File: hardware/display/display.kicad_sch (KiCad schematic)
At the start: 0 parts

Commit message: Started Display Layout
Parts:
- added C1, C10, C11, C12, C13, C14, C15, C16, C17, C18, C19, C2, C20, C21, C22, C23, C24, C25, C26, C27, C28, C29, C3, C30, C31, C32, C33, C34, C35, C36, C37, C38, C39, C4, C40, C41, C42, C43, C44, C45, C46, C47, C48, C49, C5, C50, C51, C52, C53, C54, C55, C56, C57, C58, C59, C6, C60, C61, C62, C63, C64, C65, C66, C67, C68, C69, C7, C70, C71, C72, C73, C74, C75, C76, C77, C78, C79, C8, C80, C9: 0.1uF, Capacitor_SMD:C_0504_1310Metric_Pad0.83x1.28mm_HandSolder, symbol Device:C_Small
- added C81: 1000uF, esp32_handheld:EEEFK0J332AQ, symbol Device:C_Polarized_Small_US
- added D1, D10, D100, D101, D102, D103, D104, D105, D106, D107, D108, D109, D11, D110, D111, D112, D113, D114, D115, D116, D117, D118, D119, D12, D120, D121, D122, D123, D124, D125, D126, D127, D128, D129, D13, D130, D131, D132, D133, D134, D135, D136, D137, D138, D139, D14, D140, D141, D142, D143, D144, D145, D146, D147, D148, D149, D15, D150, D151, D152, D153, D154, D155, D156, D157, D158, D159, D16, D160, D161, D162, D163, D164, D165, D166, D167, D168, D169, D17, D170, D171, D172, D173, D174, D175, D176, D177, D178, D179, D18, D180, D181, D182, D183, D184, D185, D186, D187, D188, D189, D19, D190, D191, D192, D193, D194, D195, D196, D197, D198, D199, D2, D20, D200, D201, D202, D203, D204, D205, D206, D207, D208, D209, D21, D210, D211, D212, D213, D214, D215, D216, D217, D218, D219, D22, D220, D221, D222, D223, D224, D225, D226, D227, D228, D229, D23, D230, D231, D232, D233, D234, D235, D236, D237, D238, D239, D24, D240, D241, D242, D243, D244, D245, D246, D247, D248, D249, D25, D250, D251, D252, D253, D254, D255, D256, D257, D258, D259, D26, D260, D261, D262, D263, D264, D265, D266, D267, D268, D269, D27, D270, D271, D272, D273, D274, D275, D276, D277, D278, D279, D28, D280, D281, D282, D283, D284, D285, D286, D287, D288, D289, D29, D290, D291, D292, D293, D294, D295, D296, D297, D298, D299, D3, D30, D300, D301, D302, D303, D304, D305, D306, D307, D308, D309, D31, D310, D311, D312, D313, D314, D315, D316, D317, D318, D319, D32, D320, D33, D34, D35, D36, D37, D38, D39, D4, D40, D41, D42, D43, D44, D45, D46, D47, D48, D49, D5, D50, D51, D52, D53, D54, D55, D56, D57, D58, D59, D6, D60, D61, D62, D63, D64, D65, D66, D67, D68, D69, D7, D70, D71, D72, D73, D74, D75, D76, D77, D78, D79, D8, D80, D81, D82, D83, D84, D85, D86, D87, D88, D89, D9, D90, D91, D92, D93, D94, D95, D96, D97, D98, D99: WS2812B-2020, LED_SMD:LED_WS2812B-2020_PLCC4_2.0x2.0mm, symbol LED:WS2812B-2020
- added J1: Power Connector, Connector_JST:JST_VH_B2PS-VH_1x02_P3.96mm_Horizontal, symbol Connector_Generic:Conn_01x02
- added J2: Data Connector, Connector_JST:JST_PH_S8B-PH-SM4-TB_1x08-1MP_P2.00mm_Horizontal, symbol Connector_Generic:Conn_01x08
- added R1, R2, R3, R4, R5, R6, R7, R8: 470, Resistor_SMD:R_0603_1608Metric_Pad0.98x0.95mm_HandSolder, symbol Device:R_Small_US
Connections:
- new net: D37.1 (DOUT), D38.3 (DIN)
- new net: C9.1, D36.1 (DOUT), D37.3 (DIN)
- new net: C4.1, D16.1 (DOUT), D17.3 (DIN)
- new net: D29.1 (DOUT), D30.3 (DIN)
- new net: C7.1, D28.1 (DOUT), D29.3 (DIN)
- new net: D168.3 (DIN), D176.1 (DOUT)
- new net: D176.3 (DIN), D184.1 (DOUT)
- new net: C55.1, D219.1 (DOUT), D227.3 (DIN)
- new net: D211.1 (DOUT), D219.3 (DIN)
- new net: C68.1, D256.3 (DIN), D264.1 (DOUT)
- new net: C43.1, D166.1 (DOUT)
- new net: C42.1, D164.1 (DOUT)
- new net: D164.3 (DIN), D172.1 (DOUT)
- new net: D200.3 (DIN), D208.1 (DOUT)
- new net: D208.3 (DIN), D216.1 (DOUT)
- new net: C1.1, D4.1 (DOUT), D5.3 (DIN)
- new net: D289.1 (DOUT), D297.3 (DIN)
- new net: C69.1, D281.1 (DOUT), D289.3 (DIN)
- new net: D179.1 (DOUT), D187.3 (DIN)
- new net: D171.1 (DOUT), D179.3 (DIN)
- new net: C8.1, D32.1 (DOUT), D33.3 (DIN)
- new net: D61.1 (DOUT), D63.3 (DIN)
- new net: D59.1 (DOUT), D61.3 (DIN)
- new net: D231.1 (DOUT), D239.3 (DIN)
- new net: C59.1, D223.1 (DOUT), D231.3 (DIN)
- new net: D130.3 (DIN), D132.1 (DOUT)
- new net: D132.3 (DIN), D134.1 (DOUT)
- new net: D177.1 (DOUT), D185.3 (DIN)
- new net: D169.1 (DOUT), D177.3 (DIN)
- new net: C27.1, D104.3 (DIN), D106.1 (DOUT)
- new net: D138.3 (DIN), D140.1 (DOUT)
- new net: D140.3 (DIN), D142.1 (DOUT)
- new net: C10.1, D40.1 (DOUT)
- new net: D39.1 (DOUT), D40.3 (DIN)
- new net: D167.1 (DOUT), D175.3 (DIN)
- new net: D167.3 (DIN), R8.2
- new net: D299.1 (DOUT), D307.3 (DIN)
- new net: D291.1 (DOUT), D299.3 (DIN)
- new net: D195.1 (DOUT), D203.3 (DIN)
- new net: C47.1, D187.1 (DOUT), D195.3 (DIN)
- new net: D301.1 (DOUT), D309.3 (DIN)
- new net: D293.1 (DOUT), D301.3 (DIN)
- new net: D2.1 (DOUT), D3.3 (DIN)
- new net: D1.1 (DOUT), D2.3 (DIN)
- new net: D31.1 (DOUT), D32.3 (DIN)
- new net: D30.1 (DOUT), D31.3 (DIN)
- new net: C17.1, D64.3 (DIN), D66.1 (DOUT)
- new net: C49.1, D189.1 (DOUT), D197.3 (DIN)
- new net: C77.1, D313.1 (DOUT), D314.3 (DIN)
- new net: C19.1, D72.3 (DIN), D74.1 (DOUT)
- new net: C44.1, D168.1 (DOUT)
- new net: D275.1 (DOUT), D283.3 (DIN)
- new net: D267.1 (DOUT), D275.3 (DIN)
- new net: D89.1 (DOUT), D91.3 (DIN)
- new net: C22.1, D87.1 (DOUT), D89.3 (DIN)
- new net: C24.1, D95.1 (DOUT), D97.3 (DIN)
- new net: D93.1 (DOUT), D95.3 (DIN)
- new net: C2.1, D8.1 (DOUT), D9.3 (DIN)
- new net: D23.1 (DOUT), D24.3 (DIN)
- new net: D22.1 (DOUT), D23.3 (DIN)
- new net: C23.1, D88.3 (DIN), D90.1 (DOUT)
- new net: D203.1 (DOUT), D211.3 (DIN)
- new net: D49.1 (DOUT), D51.3 (DIN)
- new net: C12.1, D47.1 (DOUT), D49.3 (DIN)
- new net: C62.1, D250.3 (DIN), D258.1 (DOUT)
- new net: D258.3 (DIN), D266.1 (DOUT)
- new net: D150.3 (DIN), D152.1 (DOUT)
- new net: C39.1, D152.3 (DIN), D154.1 (DOUT)
- new net: D273.1 (DOUT), D281.3 (DIN)
- new net: D265.1 (DOUT), D273.3 (DIN)
- new net: D309.1 (DOUT), D317.3 (DIN)
- new net: C33.1, D128.3 (DIN), D130.1 (DOUT)
- new net: D15.1 (DOUT), D16.3 (DIN)
- new net: C11.1, D42.1 (DOUT)
- new net: D25.1 (DOUT), D26.3 (DIN)
- new net: C6.1, D24.1 (DOUT), D25.3 (DIN)
- new net: D57.1 (DOUT), D59.3 (DIN)
- new net: D45.1 (DOUT), D47.3 (DIN)
- new net: D43.1 (DOUT), D45.3 (DIN)
- new net: D142.3 (DIN), D144.1 (DOUT)
- new net: D69.1 (DOUT), D71.3 (DIN)
- new net: D67.1 (DOUT), D69.3 (DIN)
- new net: C78.1, D315.1 (DOUT), D316.3 (DIN)
- new net: D121.3 (DIN), R4.2
- new net: D68.3 (DIN), D70.1 (DOUT)
- new net: D70.3 (DIN), D72.1 (DOUT)
- new net: D117.1 (DOUT), D119.3 (DIN)
- new net: D115.1 (DOUT), D117.3 (DIN)
- new net: D50.3 (DIN), D52.1 (DOUT)
- new net: D52.3 (DIN), D54.1 (DOUT)
- new net: C63.1, D251.1 (DOUT), D259.3 (DIN)
- new net: D146.3 (DIN), D148.1 (DOUT)
- new net: D148.3 (DIN), D150.1 (DOUT)
- new net: D85.1 (DOUT), D87.3 (DIN)
- new net: D83.1 (DOUT), D85.3 (DIN)
- new net: C37.1, D144.3 (DIN), D146.1 (DOUT)
- new net: D260.3 (DIN), D268.1 (DOUT)
- new net: D268.3 (DIN), D276.1 (DOUT)
- new net: C72.1, D284.3 (DIN), D292.1 (DOUT)
- new net: D292.3 (DIN), D300.1 (DOUT)
- new net: C15.1, D56.3 (DIN), D58.1 (DOUT)
- new net: D58.3 (DIN), D60.1 (DOUT)
- new net: D65.1 (DOUT), D67.3 (DIN)
- new net: C16.1, D63.1 (DOUT), D65.3 (DIN)
- new net: D161.1 (DOUT), D169.3 (DIN)
- new net: D215.1 (DOUT), D223.3 (DIN)
- new net: D207.1 (DOUT), D215.3 (DIN)
- new net: D199.1 (DOUT), D207.3 (DIN)
- new net: C31.1, D122.1 (DOUT)
- new net: D122.3 (DIN), D124.1 (DOUT)
- new net: D46.3 (DIN), D48.1 (DOUT)
- new net: C13.1, D48.3 (DIN), D50.1 (DOUT)
- new net: D6.1 (DOUT), D7.3 (DIN)
- new net: D5.1 (DOUT), D6.3 (DIN)
- new net: C32.1, D127.1 (DOUT), D129.3 (DIN)
- new net: D125.1 (DOUT), D127.3 (DIN)
- new net: D1.3 (DIN), R1.2
- new net: D174.3 (DIN), D182.1 (DOUT)
- new net: D182.3 (DIN), D190.1 (DOUT)
- new net: C50.1, D190.3 (DIN), D198.1 (DOUT)
- new net: D305.1 (DOUT), D313.3 (DIN)
- new net: C65.1, D253.1 (DOUT), D261.3 (DIN)
- new net: D245.1 (DOUT), D253.3 (DIN)
- new net: C67.1, D255.1 (DOUT), D263.3 (DIN)
- new net: D247.1 (DOUT), D255.3 (DIN)
- new net: C70.1, D282.3 (DIN), D290.1 (DOUT)
- new net: D290.3 (DIN), D298.1 (DOUT)
- new net: D17.1 (DOUT), D18.3 (DIN)
- new net: D74.3 (DIN), D76.1 (DOUT)
- new net: C53.1, D217.1 (DOUT), D225.3 (DIN)
- new net: D209.1 (DOUT), D217.3 (DIN)
- new net: C51.1, D191.1 (DOUT), D199.3 (DIN)
- new net: D183.1 (DOUT), D191.3 (DIN)
- new net: C66.1, D254.3 (DIN), D262.1 (DOUT)
- new net: D262.3 (DIN), D270.1 (DOUT)
- new net: D100.1 (DOUT), D98.3 (DIN)
- new net: D100.3 (DIN), D102.1 (DOUT)
- new net: D173.1 (DOUT), D181.3 (DIN)
- new net: D165.1 (DOUT), D173.3 (DIN)
- new net: C41.1, D162.1 (DOUT)
- new net: D162.3 (DIN), D170.1 (DOUT)
- new net: C73.1, D285.1 (DOUT), D293.3 (DIN)
- new net: D166.3 (DIN), D174.1 (DOUT)
- new net: D274.3 (DIN), D282.1 (DOUT)
- new net: D213.1 (DOUT), D221.3 (DIN)
- new net: D205.1 (DOUT), D213.3 (DIN)
- new net: D126.3 (DIN), D128.1 (DOUT)
- new net: D102.3 (DIN), D104.1 (DOUT)
- new net: D300.3 (DIN), D308.1 (DOUT)
- new net: D308.3 (DIN), D316.1 (DOUT)
- new net: D27.1 (DOUT), D28.3 (DIN)
- new net: D26.1 (DOUT), D27.3 (DIN)
- new net: C60.1, D224.3 (DIN), D232.1 (DOUT)
- new net: D232.3 (DIN), D240.1 (DOUT)
- new net: C36.1, D143.1 (DOUT), D145.3 (DIN)
- new net: D141.1 (DOUT), D143.3 (DIN)
- new net: D129.1 (DOUT), D131.3 (DIN)
- new net: D101.3 (DIN), D99.1 (DOUT)
- new net: D97.1 (DOUT), D99.3 (DIN)
- new net: D280.3 (DIN), D288.1 (DOUT)
- new net: C76.1, D288.3 (DIN), D296.1 (DOUT)
- new net: D147.1 (DOUT), D149.3 (DIN)
- new net: D145.1 (DOUT), D147.3 (DIN)
- new net: D34.1 (DOUT), D35.3 (DIN)
- new net: D33.1 (DOUT), D34.3 (DIN)
- new net: C34.1, D135.1 (DOUT), D137.3 (DIN)
- new net: D133.1 (DOUT), D135.3 (DIN)
- new net: D94.3 (DIN), D96.1 (DOUT)
- new net: C25.1, D96.3 (DIN), D98.1 (DOUT)
- new net: D66.3 (DIN), D68.1 (DOUT)
- new net: D124.3 (DIN), D126.1 (DOUT)
- new net: C75.1, D287.1 (DOUT), D295.3 (DIN)
- new net: D279.1 (DOUT), D287.3 (DIN)
- new net: C38.1, D151.1 (DOUT), D153.3 (DIN)
- new net: C14.1, D55.1 (DOUT), D57.3 (DIN)
- new net: D53.1 (DOUT), D55.3 (DIN)
- new net: C71.1, D283.1 (DOUT), D291.3 (DIN)
- new net: D302.3 (DIN), D310.1 (DOUT)
- new net: D310.3 (DIN), D318.1 (DOUT)
- new net: C52.1, D192.3 (DIN), D200.1 (DOUT)
- new net: D10.3 (DIN), D9.1 (DOUT)
- new net: D165.3 (DIN), R7.2
- new net: D298.3 (DIN), D306.1 (DOUT)
- new net: C28.1, D111.1 (DOUT), D113.3 (DIN)
- new net: D109.1 (DOUT), D111.3 (DIN)
- new net: D178.3 (DIN), D186.1 (DOUT)
- new net: C46.1, D186.3 (DIN), D194.1 (DOUT)
- new net: D240.3 (DIN), D248.1 (DOUT)
- new net: D157.1 (DOUT), D159.3 (DIN)
- new net: D155.1 (DOUT), D157.3 (DIN)
- new net: C79.1, D317.1 (DOUT), D318.3 (DIN)
- new net: D154.3 (DIN), D156.1 (DOUT)
- new net: D156.3 (DIN), D158.1 (DOUT)
- new net: D118.3 (DIN), D120.1 (DOUT)
- new net: C30.1, D119.1 (DOUT), D120.3 (DIN)
- new net: D110.3 (DIN), D112.1 (DOUT)
- new net: C29.1, D112.3 (DIN), D114.1 (DOUT)
- new net: D123.1 (DOUT), D125.3 (DIN)
- new net: D161.3 (DIN), R5.2
- new net: D172.3 (DIN), D180.1 (DOUT)
- new net: D60.3 (DIN), D62.1 (DOUT)
- new net: D62.3 (DIN), D64.1 (DOUT)
- new net: D276.3 (DIN), D284.1 (DOUT)
- new net: D226.3 (DIN), D234.1 (DOUT)
- new net: D234.3 (DIN), D242.1 (DOUT)
- new net: D241.1 (DOUT), D249.3 (DIN)
- new net: D233.1 (DOUT), D241.3 (DIN)
- new net: D237.1 (DOUT), D245.3 (DIN)
- new net: D229.1 (DOUT), D237.3 (DIN)
- new net: D163.3 (DIN), R6.2
- new net: D198.3 (DIN), D206.1 (DOUT)
- new net: C20.1, D79.1 (DOUT), D80.3 (DIN)
- new net: D77.1 (DOUT), D79.3 (DIN)
- new net: D170.3 (DIN), D178.1 (DOUT)
- new net: C21.1, D82.1 (DOUT)
- new net: D206.3 (DIN), D214.1 (DOUT)
- new net: D230.3 (DIN), D238.1 (DOUT)
- new net: D238.3 (DIN), D246.1 (DOUT)
- new net: D81.1 (DOUT), D83.3 (DIN)
- new net: D81.3 (DIN), R3.2
- new net: D134.3 (DIN), D136.1 (DOUT)
- new net: D153.1 (DOUT), D155.3 (DIN)
- new net: D105.1 (DOUT), D107.3 (DIN)
- new net: C26.1, D103.1 (DOUT), D105.3 (DIN)
- new net: D163.1 (DOUT), D171.3 (DIN)
- new net: D91.1 (DOUT), D93.3 (DIN)
- new net: D149.1 (DOUT), D151.3 (DIN)
- new net: C35.1, D136.3 (DIN), D138.1 (DOUT)
- new net: C48.1, D188.3 (DIN), D196.1 (DOUT)
- new net: D196.3 (DIN), D204.1 (DOUT)
- new net: D76.3 (DIN), D78.1 (DOUT)
- new net: D78.3 (DIN), D80.1 (DOUT)
- new net: D295.1 (DOUT), D303.3 (DIN)
- new net: D131.1 (DOUT), D133.3 (DIN)
- new net: D3.1 (DOUT), D4.3 (DIN)
- new net: D306.3 (DIN), D314.1 (DOUT)
- new net: D10.1 (DOUT), D11.3 (DIN)
- new net: C74.1, D286.3 (DIN), D294.1 (DOUT)
- new net: D294.3 (DIN), D302.1 (DOUT)
- new net: C64.1, D252.3 (DIN), D260.1 (DOUT)
- new net: D204.3 (DIN), D212.1 (DOUT)
- new net: C80.1, D319.1 (DOUT), D320.3 (DIN)
- new net: D311.1 (DOUT), D319.3 (DIN)
- new net: D277.1 (DOUT), D285.3 (DIN)
- new net: D278.3 (DIN), D286.1 (DOUT)
- new net: D236.3 (DIN), D244.1 (DOUT)
- new net: D244.3 (DIN), D252.1 (DOUT)
- new net: C45.1, D185.1 (DOUT), D193.3 (DIN)
- new net: D271.1 (DOUT), D279.3 (DIN)
- new net: D263.1 (DOUT), D271.3 (DIN)
- new net: D248.3 (DIN), D256.1 (DOUT)
- new net: D264.3 (DIN), D272.1 (DOUT)
- new net: D272.3 (DIN), D280.1 (DOUT)
- new net: C61.1, D249.1 (DOUT), D257.3 (DIN)
- new net: D307.1 (DOUT), D315.3 (DIN)
- new net: D257.1 (DOUT), D265.3 (DIN)
- new net: D181.1 (DOUT), D189.3 (DIN)
- new net: D184.3 (DIN), D192.1 (DOUT)
- new net: D303.1 (DOUT), D311.3 (DIN)
- new net: D114.3 (DIN), D116.1 (DOUT)
- new net: D121.1 (DOUT), D123.3 (DIN)
- new net: D197.1 (DOUT), D205.3 (DIN)
- new net: D113.1 (DOUT), D115.3 (DIN)
- new net: D216.3 (DIN), D224.1 (DOUT)
- new net: D42.3 (DIN), D44.1 (DOUT)
- new net: D44.3 (DIN), D46.1 (DOUT)
- new net: D225.1 (DOUT), D233.3 (DIN)
- new net: D90.3 (DIN), D92.1 (DOUT)
- new net: D92.3 (DIN), D94.1 (DOUT)
- new net: C58.1, D222.3 (DIN), D230.1 (DOUT)
- new net: D108.3 (DIN), D110.1 (DOUT)
- new net: C57.1, D221.1 (DOUT), D229.3 (DIN)
- new net: D139.1 (DOUT), D141.3 (DIN)
- new net: D21.1 (DOUT), D22.3 (DIN)
- new net: C5.1, D20.1 (DOUT), D21.3 (DIN)
- new net: D38.1 (DOUT), D39.3 (DIN)
- new net: D175.1 (DOUT), D183.3 (DIN)
- new net: D75.1 (DOUT), D77.3 (DIN)
- new net: D106.3 (DIN), D108.1 (DOUT)
- new net: D259.1 (DOUT), D267.3 (DIN)
- new net: D235.1 (DOUT), D243.3 (DIN)
- new net: D227.1 (DOUT), D235.3 (DIN)
- new net: D19.1 (DOUT), D20.3 (DIN)
- new net: D18.1 (DOUT), D19.3 (DIN)
- new net: D212.3 (DIN), D220.1 (DOUT)
- new net: C56.1, D220.3 (DIN), D228.1 (DOUT)
- new net: C18.1, D71.1 (DOUT), D73.3 (DIN)
- new net: D73.1 (DOUT), D75.3 (DIN)
- new net: D297.1 (DOUT), D305.3 (DIN)
- new net: D180.3 (DIN), D188.1 (DOUT)
- new net: D35.1 (DOUT), D36.3 (DIN)
- new net: D14.1 (DOUT), D15.3 (DIN)
- new net: D202.3 (DIN), D210.1 (DOUT)
- new net: D210.3 (DIN), D218.1 (DOUT)
- new net: D107.1 (DOUT), D109.3 (DIN)
- new net: D194.3 (DIN), D202.1 (DOUT)
- new net: D243.1 (DOUT), D251.3 (DIN)
- new net: D41.3 (DIN), R2.2
- new net: D246.3 (DIN), D254.1 (DOUT)
- new net: D158.3 (DIN), D160.1 (DOUT)
- new net: D41.1 (DOUT), D43.3 (DIN)
- new net: C40.1, D159.1 (DOUT), D160.3 (DIN)
- new net: D11.1 (DOUT), D12.3 (DIN)
- new net: D116.3 (DIN), D118.1 (DOUT)
- new net: D270.3 (DIN), D278.1 (DOUT)
- new net: D312.3 (DIN), D320.1 (DOUT)
- new net: D86.3 (DIN), D88.1 (DOUT)
- new net: D54.3 (DIN), D56.1 (DOUT)
- new net: C3.1, D12.1 (DOUT), D13.3 (DIN)
- new net: D101.1 (DOUT), D103.3 (DIN)
- new net: D51.1 (DOUT), D53.3 (DIN)
- new net: D214.3 (DIN), D222.1 (DOUT)
- new net: C54.1, D218.3 (DIN), D226.1 (DOUT)
- new net: D82.3 (DIN), D84.1 (DOUT)
- new net: D228.3 (DIN), D236.1 (DOUT)
- new net: D201.1 (DOUT), D209.3 (DIN)
- new net: D193.1 (DOUT), D201.3 (DIN)
- new net: D304.3 (DIN), D312.1 (DOUT)
- new net: D261.1 (DOUT), D269.3 (DIN)
- new net: D242.3 (DIN), D250.1 (DOUT)
- new net: D84.3 (DIN), D86.1 (DOUT)
- new net: D239.1 (DOUT), D247.3 (DIN)
- new net: D7.1 (DOUT), D8.3 (DIN)
- new net: D137.1 (DOUT), D139.3 (DIN)
- new net: D266.3 (DIN), D274.1 (DOUT)
- new net: D269.1 (DOUT), D277.3 (DIN)
- new net: D13.1 (DOUT), D14.3 (DIN)
- new net: D296.3 (DIN), D304.1 (DOUT)
- new net DIN1: J2.1 (Pin_1), R1.1
- new net DIN2: J2.2 (Pin_2), R2.1
- new net DIN3: J2.3 (Pin_3), R3.1
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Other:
- note added: "Connectors"
- company: (none) -> "Gamers"
- title: (none) -> Display Board

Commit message: Arranged LEDs
Arranged NeoPixel footprints and handled schematic/PCB link and designations
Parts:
- removed C5: 0.1uF, Capacitor_SMD:C_0504_1310Metric_Pad0.83x1.28mm_HandSolder, symbol Device:C_Small
- added C1: 0.1uF, Capacitor_SMD:C_0402_1005Metric_Pad0.74x0.62mm_HandSolder, symbol Device:C_Small
- C10, C11, C12, C13, C14, C15, C16, C17, C18, C19, C20, C21, C22, C23, C24, C25, C26, C27, C28, C29, C30, C31, C32, C33, C34, C35, C36, C37, C38, C39, C40, C41, C42, C43, C44, C45, C46, C47, C48, C49, C50, C51, C52, C53, C54, C55, C56, C57, C58, C59, C6, C60, C61, C62, C63, C64, C65, C66, C67, C68, C69, C7, C70, C71, C72, C73, C74, C75, C76, C77, C78, C79, C8, C80, C9: footprint Capacitor_SMD:C_0504_1310Metric_Pad0.83x1.28mm_HandSolder -> Capacitor_SMD:C_0402_1005Metric_Pad0.74x0.62mm_HandSolder
- C2: renamed from C1; footprint Capacitor_SMD:C_0504_1310Metric_Pad0.83x1.28mm_HandSolder -> Capacitor_SMD:C_0402_1005Metric_Pad0.74x0.62mm_HandSolder
- C3: renamed from C2; footprint Capacitor_SMD:C_0504_1310Metric_Pad0.83x1.28mm_HandSolder -> Capacitor_SMD:C_0402_1005Metric_Pad0.74x0.62mm_HandSolder
- C4: renamed from C3; footprint Capacitor_SMD:C_0504_1310Metric_Pad0.83x1.28mm_HandSolder -> Capacitor_SMD:C_0402_1005Metric_Pad0.74x0.62mm_HandSolder
- C5: renamed from C4; footprint Capacitor_SMD:C_0504_1310Metric_Pad0.83x1.28mm_HandSolder -> Capacitor_SMD:C_0402_1005Metric_Pad0.74x0.62mm_HandSolder
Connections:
- net GND: now also C1.2
- net at D36.1 (DOUT), D37.3 (DIN): now also C10.1; no longer C9.1
- net at D28.1 (DOUT), D29.3 (DIN): now also C8.1; no longer C7.1
- net at D176.1 (DOUT): now also C45.1, D177.3 (DIN); no longer D168.3 (DIN)
- net at D176.3 (DIN): now also D175.1 (DOUT); no longer D184.1 (DOUT)
- net at D219.3 (DIN): now also D218.1 (DOUT); no longer D211.1 (DOUT)
- net at D166.1 (DOUT): now also D167.3 (DIN); no longer C43.1
- net at C42.1, D164.1 (DOUT): now also D165.3 (DIN)
- net at D164.3 (DIN): now also D163.1 (DOUT); no longer D172.1 (DOUT)
- net at D200.3 (DIN): now also D199.1 (DOUT); no longer D208.1 (DOUT)
- net at D216.1 (DOUT): now also C55.1, D217.3 (DIN); no longer D208.3 (DIN)
- net at D297.3 (DIN): now also C75.1, D296.1 (DOUT); no longer D289.1 (DOUT)
- net at D179.1 (DOUT): now also D180.3 (DIN); no longer D187.3 (DIN)
- net at D171.1 (DOUT): now also D172.3 (DIN); no longer D179.3 (DIN)
- net at D32.1 (DOUT), D33.3 (DIN): now also C9.1; no longer C8.1
- net at D63.3 (DIN): now also D62.1 (DOUT); no longer D61.1 (DOUT)
- net at D61.3 (DIN): now also C16.1, D60.1 (DOUT); no longer D59.1 (DOUT)
- net at D239.3 (DIN): now also D238.1 (DOUT); no longer D231.1 (DOUT)
- net at D130.3 (DIN): now also D129.1 (DOUT); no longer D132.1 (DOUT)
- net at D134.1 (DOUT): now also D135.3 (DIN); no longer D132.3 (DIN)
- net at D185.3 (DIN): now also C47.1, D184.1 (DOUT); no longer D177.1 (DOUT)
- net at D169.1 (DOUT): now also D170.3 (DIN); no longer D177.3 (DIN)
- net at D140.1 (DOUT): now also C36.1, D141.3 (DIN); no longer D138.3 (DIN)
- net at D142.1 (DOUT): now also D143.3 (DIN); no longer D140.3 (DIN)
- net at D40.1 (DOUT): no longer C10.1
- net at D175.3 (DIN): now also D174.1 (DOUT); no longer D167.1 (DOUT)
- net at R8.2: now also C71.1, D281.3 (DIN); no longer D167.3 (DIN)
- net at D299.1 (DOUT): now also D300.3 (DIN); no longer D307.3 (DIN)
- net at D291.1 (DOUT): now also D292.3 (DIN); no longer D299.3 (DIN)
- net at D195.1 (DOUT): now also D196.3 (DIN); no longer D203.3 (DIN)
- net at D309.3 (DIN): now also C78.1, D308.1 (DOUT); no longer D301.1 (DOUT)
- net at D301.3 (DIN): now also C76.1, D300.1 (DOUT); no longer D293.1 (DOUT)
- net at D313.1 (DOUT), D314.3 (DIN): no longer C77.1
- net at C44.1: now also D172.1 (DOUT), D173.3 (DIN); no longer D168.1 (DOUT)
- net at D283.3 (DIN): now also D282.1 (DOUT); no longer D275.1 (DOUT)
- net at D267.1 (DOUT): now also D268.3 (DIN); no longer D275.3 (DIN)
- net at D91.3 (DIN): now also D90.1 (DOUT); no longer D89.1 (DOUT)
- net at D95.3 (DIN): now also D94.1 (DOUT); no longer D93.1 (DOUT)
- net at D203.1 (DOUT): now also D204.3 (DIN); no longer D211.3 (DIN)
- net at D51.3 (DIN): now also D50.1 (DOUT); no longer D49.1 (DOUT)
- net at D258.3 (DIN): now also D257.1 (DOUT); no longer D266.1 (DOUT)
- net at D150.3 (DIN): now also D149.1 (DOUT); no longer D152.1 (DOUT)
- net at D273.1 (DOUT): now also D274.3 (DIN); no longer D281.3 (DIN)
- net at D273.3 (DIN): now also C69.1, D272.1 (DOUT); no longer D265.1 (DOUT)
- net at D317.3 (DIN): now also C80.1, D316.1 (DOUT); no longer D309.1 (DOUT)
- net at C11.1: now also D41.3 (DIN), R2.2; no longer D42.1 (DOUT)
- net at D24.1 (DOUT), D25.3 (DIN): now also C7.1; no longer C6.1
- net at D59.3 (DIN): now also D58.1 (DOUT); no longer D57.1 (DOUT)
- net at D47.3 (DIN): now also D46.1 (DOUT); no longer D45.1 (DOUT)
- net at D45.3 (DIN): now also C12.1, D44.1 (DOUT); no longer D43.1 (DOUT)
- net at D142.3 (DIN): now also D141.1 (DOUT); no longer D144.1 (DOUT)
- net at D69.1 (DOUT): now also D70.3 (DIN); no longer D71.3 (DIN)
- net at D69.3 (DIN): now also C18.1, D68.1 (DOUT); no longer D67.1 (DOUT)
- net at D315.1 (DOUT), D316.3 (DIN): no longer C78.1
- net at D121.3 (DIN), R4.2: now also C31.1
- net at D68.3 (DIN): now also D67.1 (DOUT); no longer D70.1 (DOUT)
- net at D72.1 (DOUT): now also C19.1, D73.3 (DIN); no longer D70.3 (DIN)
- net at D119.3 (DIN): now also D118.1 (DOUT); no longer D117.1 (DOUT)
- net at D115.1 (DOUT): now also D116.3 (DIN); no longer D117.3 (DIN)
- net at D50.3 (DIN): now also D49.1 (DOUT); no longer D52.1 (DOUT)
- net at D54.1 (DOUT): now also D55.3 (DIN); no longer D52.3 (DIN)
- net at D146.3 (DIN): now also D145.1 (DOUT); no longer D148.1 (DOUT)
- net at D148.3 (DIN): now also D147.1 (DOUT); no longer D150.1 (DOUT)
- net at D87.3 (DIN): now also D86.1 (DOUT); no longer D85.1 (DOUT)
- net at D83.1 (DOUT): now also D84.3 (DIN); no longer D85.3 (DIN)
- net at D260.3 (DIN): now also D259.1 (DOUT); no longer D268.1 (DOUT)
- net at D276.1 (DOUT): now also C70.1, D277.3 (DIN); no longer D268.3 (DIN)
- net at D58.3 (DIN): now also D57.1 (DOUT); no longer D60.1 (DOUT)
- net at D65.1 (DOUT): now also D66.3 (DIN); no longer D67.3 (DIN)
- net at D161.1 (DOUT): now also D162.3 (DIN); no longer D169.3 (DIN)
- net at D215.1 (DOUT): now also D216.3 (DIN); no longer D223.3 (DIN)
- net at D215.3 (DIN): now also D214.1 (DOUT); no longer D207.1 (DOUT)
- net at D207.3 (DIN): now also D206.1 (DOUT); no longer D199.1 (DOUT)
- net at D122.1 (DOUT): now also D123.3 (DIN); no longer C31.1
- net at D122.3 (DIN): now also D121.1 (DOUT); no longer D124.1 (DOUT)
- net at D48.1 (DOUT): now also C13.1, D49.3 (DIN); no longer D46.3 (DIN)
- net at D127.3 (DIN): now also D126.1 (DOUT); no longer D125.1 (DOUT)
- net at D1.3 (DIN), R1.2: now also C1.1
- net at D182.1 (DOUT): now also D183.3 (DIN); no longer D174.3 (DIN)
- net at D182.3 (DIN): now also D181.1 (DOUT); no longer D190.1 (DOUT)
- net at D313.3 (DIN): now also C79.1, D312.1 (DOUT); no longer D305.1 (DOUT)
- net at D245.1 (DOUT): now also D246.3 (DIN); no longer D253.3 (DIN)
- net at D247.1 (DOUT): now also D248.3 (DIN); no longer D255.3 (DIN)
- net at D290.3 (DIN): now also D289.1 (DOUT); no longer D298.1 (DOUT)
- net at D76.1 (DOUT): now also C20.1, D77.3 (DIN); no longer D74.3 (DIN)
- net at D209.1 (DOUT): now also D210.3 (DIN); no longer D217.3 (DIN)
- net at D183.1 (DOUT): now also D184.3 (DIN); no longer D191.3 (DIN)
- net at D270.1 (DOUT): now also D271.3 (DIN); no longer D262.3 (DIN)
- net at D98.3 (DIN): now also D97.1 (DOUT); no longer D100.1 (DOUT)
- net at D102.1 (DOUT): now also D103.3 (DIN); no longer D100.3 (DIN)
- net at D181.3 (DIN): now also C46.1, D180.1 (DOUT); no longer D173.1 (DOUT)
- net at D165.1 (DOUT): now also D166.3 (DIN); no longer D173.3 (DIN)
- net at D162.1 (DOUT): now also D163.3 (DIN); no longer C41.1
- net at D170.1 (DOUT): now also D171.3 (DIN); no longer D162.3 (DIN)
- net at D213.1 (DOUT): now also D214.3 (DIN); no longer D221.3 (DIN)
- net at D213.3 (DIN): now also C54.1, D212.1 (DOUT); no longer D205.1 (DOUT)
- net at D126.3 (DIN): now also D125.1 (DOUT); no longer D128.1 (DOUT)
- net at D104.1 (DOUT): now also C27.1, D105.3 (DIN); no longer D102.3 (DIN)
- net at D308.3 (DIN): now also D307.1 (DOUT); no longer D316.1 (DOUT)
- net at D240.1 (DOUT): no longer D232.3 (DIN)
- net at D131.3 (DIN): now also D130.1 (DOUT); no longer D129.1 (DOUT)
- net at D101.3 (DIN): now also C26.1, D100.1 (DOUT); no longer D99.1 (DOUT)
- net at D99.3 (DIN): now also D98.1 (DOUT); no longer D97.1 (DOUT)
- net at D288.1 (DOUT): now also C73.1, D289.3 (DIN); no longer D280.3 (DIN)
- net at D149.3 (DIN): now also C38.1, D148.1 (DOUT); no longer D147.1 (DOUT)
- net at D147.3 (DIN): now also D146.1 (DOUT); no longer D145.1 (DOUT)
- net at D133.1 (DOUT): now also D134.3 (DIN); no longer D135.3 (DIN)
- net at D96.1 (DOUT): now also C25.1, D97.3 (DIN); no longer D94.3 (DIN)
- net at D124.3 (DIN): now also D123.1 (DOUT); no longer D126.1 (DOUT)
- net at D287.3 (DIN): now also D286.1 (DOUT); no longer D279.1 (DOUT)
- net at D53.1 (DOUT): now also D54.3 (DIN); no longer D55.3 (DIN)
- net at D302.3 (DIN): now also D301.1 (DOUT); no longer D310.1 (DOUT)
- net at D318.1 (DOUT): now also D319.3 (DIN); no longer D310.3 (DIN)
- net at R7.2: now also C61.1, D241.3 (DIN); no longer D165.3 (DIN)
- net at D306.1 (DOUT): now also D307.3 (DIN); no longer D298.3 (DIN)
- net at D111.3 (DIN): now also D110.1 (DOUT); no longer D109.1 (DOUT)
- net at D186.1 (DOUT): now also D187.3 (DIN); no longer D178.3 (DIN)
- net at D248.1 (DOUT): now also C63.1, D249.3 (DIN); no longer D240.3 (DIN)
- net at D159.3 (DIN): now also D158.1 (DOUT); no longer D157.1 (DOUT)
- net at D155.1 (DOUT): now also D156.3 (DIN); no longer D157.3 (DIN)
- net at D317.1 (DOUT), D318.3 (DIN): no longer C79.1
- net at D156.1 (DOUT): now also C40.1, D157.3 (DIN); no longer D154.3 (DIN)
- net at D118.3 (DIN): now also D117.1 (DOUT); no longer D120.1 (DOUT)
- net at D119.1 (DOUT), D120.3 (DIN): no longer C30.1
- net at D112.1 (DOUT): now also C29.1, D113.3 (DIN); no longer D110.3 (DIN)
- net at D125.3 (DIN): now also C32.1, D124.1 (DOUT); no longer D123.1 (DOUT)
- net at D161.3 (DIN), R5.2: now also C41.1
- net at D60.3 (DIN): now also D59.1 (DOUT); no longer D62.1 (DOUT)
- net at D64.1 (DOUT): now also C17.1, D65.3 (DIN); no longer D62.3 (DIN)
- net at D284.1 (DOUT): now also C72.1, D285.3 (DIN); no longer D276.3 (DIN)
- net at D226.3 (DIN): now also D225.1 (DOUT); no longer D234.1 (DOUT)
- net at D242.1 (DOUT): now also D243.3 (DIN); no longer D234.3 (DIN)
- net at D241.1 (DOUT): now also D242.3 (DIN); no longer D249.3 (DIN)
- net at D233.1 (DOUT): now also D234.3 (DIN); no longer D241.3 (DIN)
- net at D237.1 (DOUT): now also D238.3 (DIN); no longer D245.3 (DIN)
- net at D229.1 (DOUT): now also D230.3 (DIN); no longer D237.3 (DIN)
- net at R6.2: now also C51.1, D201.3 (DIN); no longer D163.3 (DIN)
- net at D198.3 (DIN): now also D197.1 (DOUT); no longer D206.1 (DOUT)
- net at D79.1 (DOUT), D80.3 (DIN): no longer C20.1
- net at D77.1 (DOUT): now also D78.3 (DIN); no longer D79.3 (DIN)
- net at D178.1 (DOUT): now also D179.3 (DIN); no longer D170.3 (DIN)
- net at C21.1: now also D81.3 (DIN), R3.2; no longer D82.1 (DOUT)
- net at D206.3 (DIN): now also D205.1 (DOUT); no longer D214.1 (DOUT)
- net at D246.1 (DOUT): now also D247.3 (DIN); no longer D238.3 (DIN)
- net at D81.1 (DOUT): now also D82.3 (DIN); no longer D83.3 (DIN)
- net at D136.1 (DOUT): now also C35.1, D137.3 (DIN); no longer D134.3 (DIN)
- net at D155.3 (DIN): now also D154.1 (DOUT); no longer D153.1 (DOUT)
- net at D107.3 (DIN): now also D106.1 (DOUT); no longer D105.1 (DOUT)
- net at D91.1 (DOUT): now also D92.3 (DIN); no longer D93.3 (DIN)
- net at D151.3 (DIN): now also D150.1 (DOUT); no longer D149.1 (DOUT)
- net at D204.1 (DOUT): now also C52.1, D205.3 (DIN); no longer D196.3 (DIN)
- net at D78.1 (DOUT): now also D79.3 (DIN); no longer D76.3 (DIN)
- net at D80.1 (DOUT): no longer D78.3 (DIN)
- net at D295.1 (DOUT): now also D296.3 (DIN); no longer D303.3 (DIN)
- net at D133.3 (DIN): now also C34.1, D132.1 (DOUT); no longer D131.1 (DOUT)
- net at D314.1 (DOUT): now also D315.3 (DIN); no longer D306.3 (DIN)
- net at D294.3 (DIN): now also D293.1 (DOUT); no longer D302.1 (DOUT)
- net at D319.1 (DOUT), D320.3 (DIN): no longer C80.1
- net at D311.1 (DOUT): now also D312.3 (DIN); no longer D319.3 (DIN)
- net at D277.1 (DOUT): now also D278.3 (DIN); no longer D285.3 (DIN)
- net at D236.3 (DIN): now also D235.1 (DOUT); no longer D244.1 (DOUT)
- net at D244.3 (DIN): now also D243.1 (DOUT); no longer D252.1 (DOUT)
- net at D271.1 (DOUT): now also D272.3 (DIN); no longer D279.3 (DIN)
- net at D263.1 (DOUT): now also D264.3 (DIN); no longer D271.3 (DIN)
- new net: D198.1 (DOUT), D199.3 (DIN)
- new net: D283.1 (DOUT), D284.3 (DIN)
- new net: D63.1 (DOUT), D64.3 (DIN)
- new net: D103.1 (DOUT), D104.3 (DIN)
- new net: D167.1 (DOUT), D168.3 (DIN)
- new net: D66.1 (DOUT), D67.3 (DIN)
- new net: D230.1 (DOUT), D231.3 (DIN)
- new net: C66.1, D260.1 (DOUT), D261.3 (DIN)
- new net: D249.1 (DOUT), D250.3 (DIN)
- new net: D135.1 (DOUT), D136.3 (DIN)
- new net: D219.1 (DOUT), D220.3 (DIN)
- new net: D287.1 (DOUT), D288.3 (DIN)
- new net: D290.1 (DOUT), D291.3 (DIN)
- new net: C74.1, D292.1 (DOUT), D293.3 (DIN)
- new net: D309.1 (DOUT), D310.3 (DIN)
- new net: D285.1 (DOUT), D286.3 (DIN)
- new net: D71.1 (DOUT), D72.3 (DIN)
- new net: D258.1 (DOUT), D259.3 (DIN)
- new net: D47.1 (DOUT), D48.3 (DIN)
- new net: D109.1 (DOUT), D110.3 (DIN)
- new net: D253.1 (DOUT), D254.3 (DIN)
- new net: C64.1, D252.1 (DOUT), D253.3 (DIN)
- new net: D95.1 (DOUT), D96.3 (DIN)
- new net: D207.1 (DOUT), D208.3 (DIN)
- new net: D223.1 (DOUT), D224.3 (DIN)
- new net: D194.1 (DOUT), D195.3 (DIN)
- new net: D251.1 (DOUT), D252.3 (DIN)
- new net: C58.1, D228.1 (DOUT), D229.3 (DIN)
- new net: D227.1 (DOUT), D228.3 (DIN)
- new net: C33.1, D128.1 (DOUT), D129.3 (DIN)
- new net: D127.1 (DOUT), D128.3 (DIN)
- new net: D82.1 (DOUT), D83.3 (DIN)
- new net: D226.1 (DOUT), D227.3 (DIN)
- new net: C50.1, D196.1 (DOUT), D197.3 (DIN)
- new net: D143.1 (DOUT), D144.3 (DIN)
- new net: D87.1 (DOUT), D88.3 (DIN)
- new net: D191.1 (DOUT), D192.3 (DIN)
- new net: D190.1 (DOUT), D191.3 (DIN)
- new net: C23.1, D88.1 (DOUT), D89.3 (DIN)
- new net: D298.1 (DOUT), D299.3 (DIN)
- new net: D221.1 (DOUT), D222.3 (DIN)
- new net: D185.1 (DOUT), D186.3 (DIN)
- new net: D217.1 (DOUT), D218.3 (DIN)
- new net: D187.1 (DOUT), D188.3 (DIN)
- new net: D151.1 (DOUT), D152.3 (DIN)
- new net: D157.1 (DOUT), D158.3 (DIN)
- new net: C37.1, D144.1 (DOUT), D145.3 (DIN)
- new net: D45.1 (DOUT), D46.3 (DIN)
- new net: D105.1 (DOUT), D106.3 (DIN)
- new net: D51.1 (DOUT), D52.3 (DIN)
- new net: D279.1 (DOUT), D280.3 (DIN)
- new net: D278.1 (DOUT), D279.3 (DIN)
- new net: D55.1 (DOUT), D56.3 (DIN)
- new net: C62.1, D244.1 (DOUT), D245.3 (DIN)
- new net: C56.1, D220.1 (DOUT), D221.3 (DIN)
- new net: D100.3 (DIN), D99.1 (DOUT)
- new net: D111.1 (DOUT), D112.3 (DIN)
- new net: D173.1 (DOUT), D174.3 (DIN)
- new net: C43.1, D168.1 (DOUT), D169.3 (DIN)
- new net: D177.1 (DOUT), D178.3 (DIN)
- new net: D294.1 (DOUT), D295.3 (DIN)
- new net: D305.1 (DOUT), D306.3 (DIN)
- new net: D210.1 (DOUT), D211.3 (DIN)
- new net: D302.1 (DOUT), D303.3 (DIN)
- new net: C68.1, D268.1 (DOUT), D269.3 (DIN)
- new net: D281.1 (DOUT), D282.3 (DIN)
- new net: D131.1 (DOUT), D132.3 (DIN)
- new net: D310.1 (DOUT), D311.3 (DIN)
- new net: D93.1 (DOUT), D94.3 (DIN)
- new net: D74.1 (DOUT), D75.3 (DIN)
- new net: D113.1 (DOUT), D114.3 (DIN)
- new net: D275.1 (DOUT), D276.3 (DIN)
- new net: D274.1 (DOUT), D275.3 (DIN)
- new net: D137.1 (DOUT), D138.3 (DIN)
- new net: D255.1 (DOUT), D256.3 (DIN)
- new net: D153.1 (DOUT), D154.3 (DIN)
- new net: C39.1, D152.1 (DOUT), D153.3 (DIN)
- new net: D70.1 (DOUT), D71.3 (DIN)
- new net: D189.1 (DOUT), D190.3 (DIN)
- new net: D61.1 (DOUT), D62.3 (DIN)
- new net: D89.1 (DOUT), D90.3 (DIN)
- new net: D231.1 (DOUT), D232.3 (DIN)
- new net: D262.1 (DOUT), D263.3 (DIN)
- new net: D297.1 (DOUT), D298.3 (DIN)
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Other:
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
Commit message: Display Traces and Connector Placement
Board is all connected and has no errors
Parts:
- J2: footprint Connector_JST:JST_PH_S8B-PH-SM4-TB_1x08-1MP_P2.00mm_Horizontal -> Connector_JST:JST_PH_S8B-PH-K_1x08_P2.00mm_Horizontal
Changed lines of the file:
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@@
 			)
 		)
-		(property "Footprint" "Connector_JST:JST_PH_S8B-PH-SM4-TB_1x08-1MP_P2.00mm_Horizontal"
+		(property "Footprint" "Connector_JST:JST_PH_S8B-PH-K_1x08_P2.00mm_Horizontal"
 			(at 509.27 218.44 0)
 			(effects

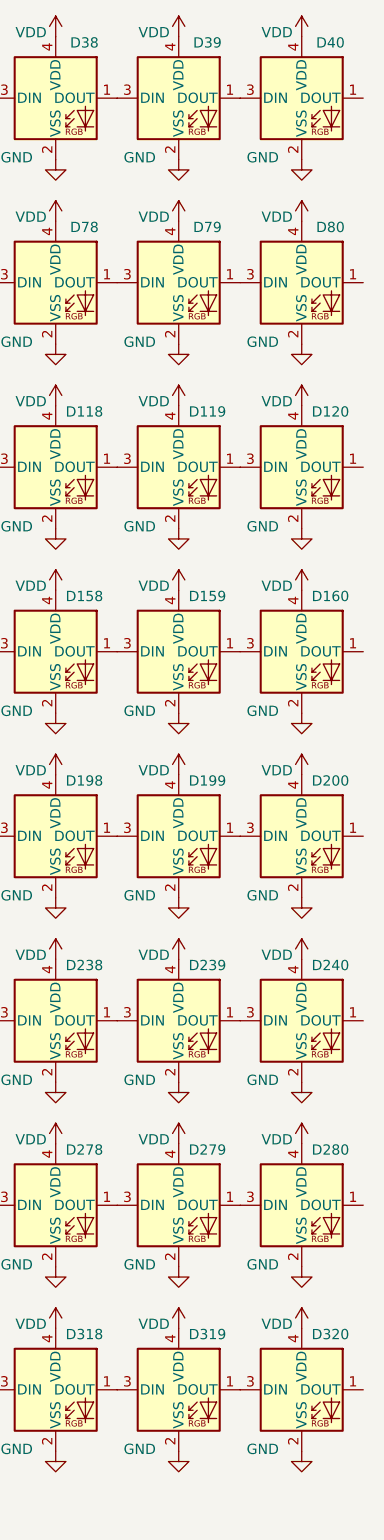
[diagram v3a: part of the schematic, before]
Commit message: Will Meeting
Added JLC constraints
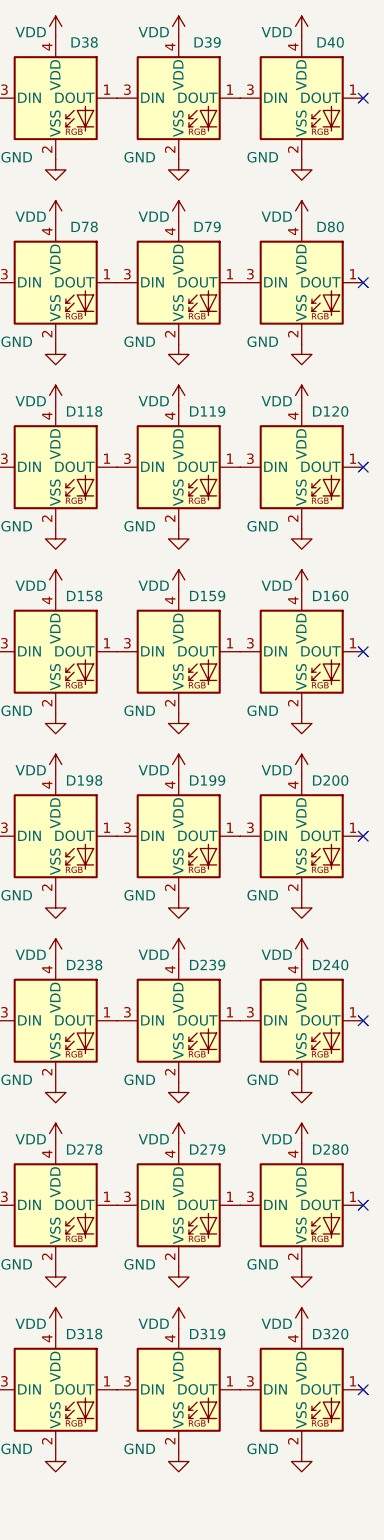
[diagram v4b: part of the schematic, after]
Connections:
- no-connect marks 0 -> 8
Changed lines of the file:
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@@
 		(color 0 0 0 0)
+	)
+	(no_connect
+		(at 638.81 167.64)
+	)
+	(no_connect
+		(at 638.81 99.06)
+	)
+	(no_connect
+		(at 638.81 30.48)
+	)
+	(no_connect
+		(at 638.81 76.2)
+	)
+	(no_connect
+		(at 638.81 53.34)
+	)
+	(no_connect
+		(at 638.81 121.92)
+	)
+	(no_connect
+		(at 638.81 190.5)
+	)
+	(no_connect
+		(at 638.81 144.78)
 	)
 	(wire

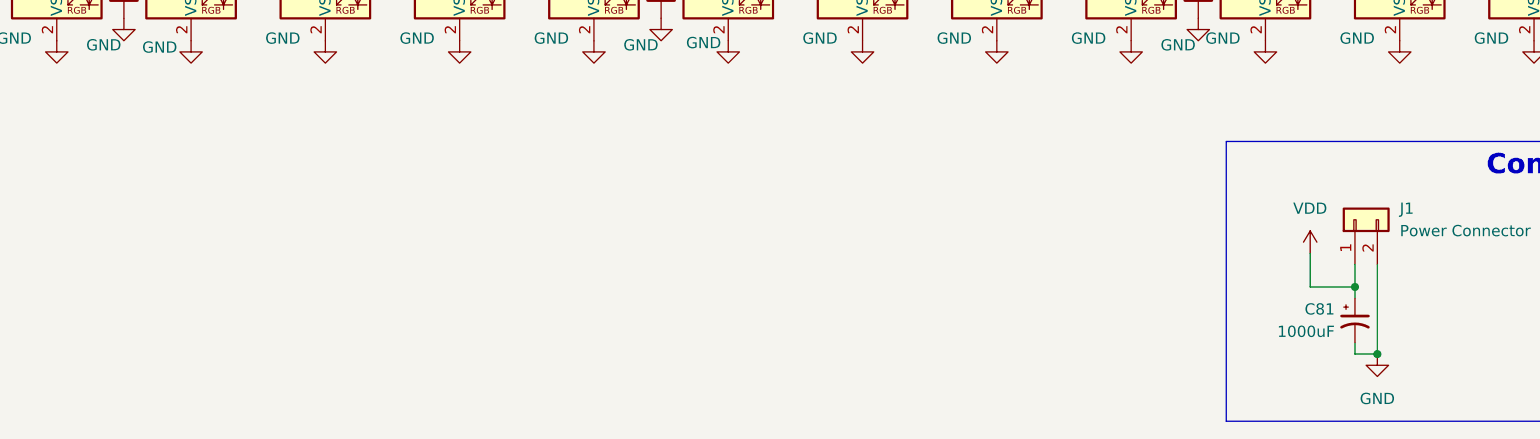
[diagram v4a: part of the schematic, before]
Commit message: Added assembly part numbers and schematic caps
Linked LCSC part numbers for LEDs, decoupling caps, and data resistors.

Added 10, 100uF caps in schematic, but footprints are needed still.
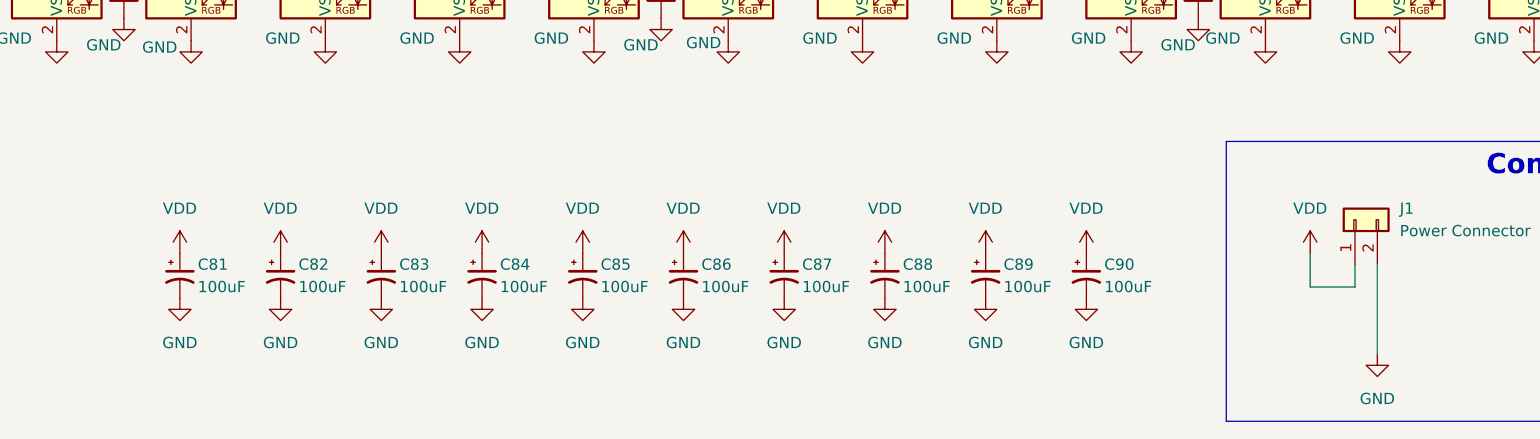
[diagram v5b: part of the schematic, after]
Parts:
- added C82, C83, C84, C85, C86, C87, C88, C89, C90: 100uF, symbol Device:C_Polarized_Small_US
- C81: value 1000uF -> 100uF; footprint esp32_handheld:EEEFK0J332AQ -> (none)
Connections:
- net GND: now also C82.2, C83.2, C84.2, C85.2, C86.2, C87.2, C88.2, C89.2, C90.2
- net VDD: now also C82.1, C83.1, C84.1, C85.1, C86.1, C87.1, C88.1, C89.1, C90.1

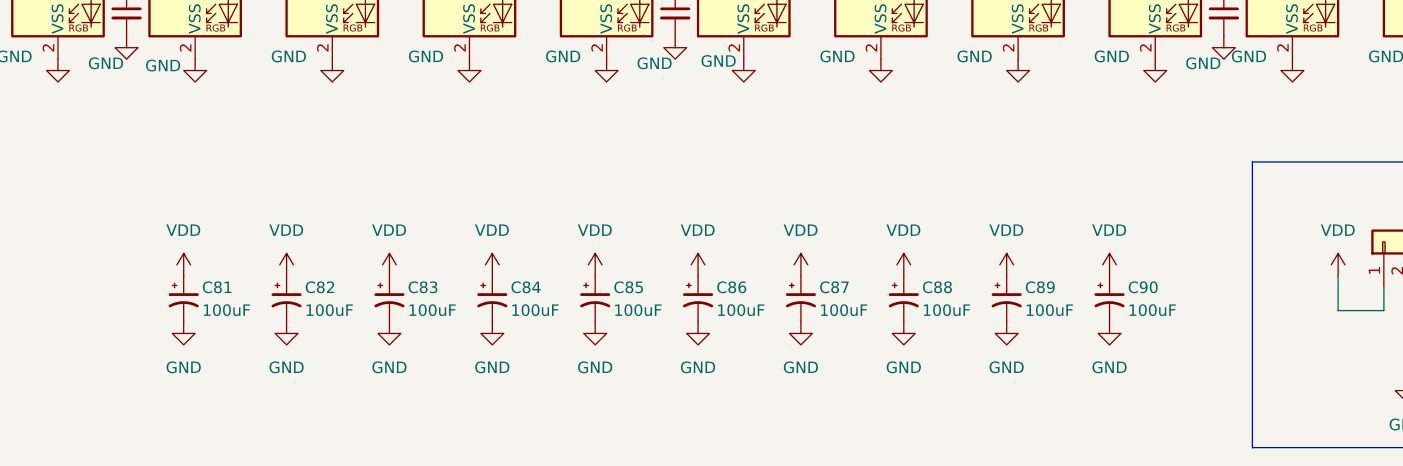
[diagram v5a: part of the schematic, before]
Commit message: Added 100uF cap symbols and footprints
Added symbols in schematic and footprints in PCB. Caps need layout and routing.
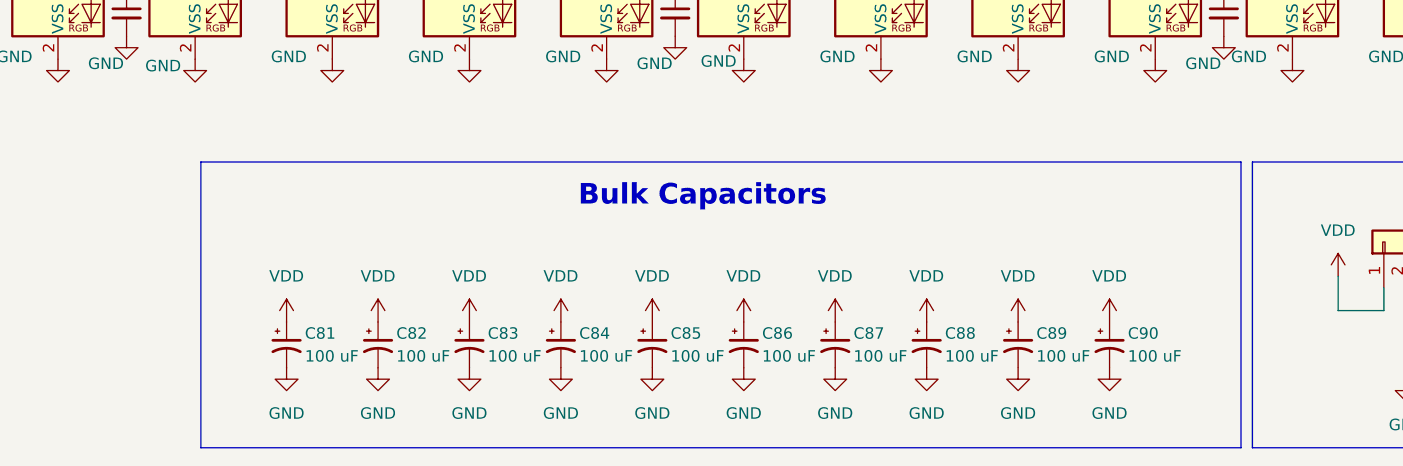
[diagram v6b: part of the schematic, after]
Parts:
- C81, C82, C83, C84, C85, C86, C87, C88, C89, C90: value 100uF -> 100 uF; footprint (none) -> esp32_handheld:CAP_TAJ-D- 2917-S_AVX
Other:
- note added: "Bulk Capacitors"
